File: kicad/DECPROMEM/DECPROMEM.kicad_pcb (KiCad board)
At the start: 2 copper layers, 127 x 132.1 mm, 138 parts, among them J10 BDAL08, J100 A15, J101 A16, J102 A17, J103 A18, J104 A19, J105 A20, J106 A21, J107 +5V, J11 BDAL09, J12 BDAL10, J13 BDAL11, J14 BDAL12, J15 BDAL13, J16 BDAL14, J17 BDAL15, J18 BDAL16, J19 BDAL17, J2 BDAL00, J20 BDAL18, J21 BDAL19, J22 BDAL20, J23 BDAL21, J24 BRPLYL, J25 BMDENL, J26 BWRITEL, J27 BWLBL, J28 BWHBL, J29 BSDENL, J3 BDAL01, J30 SSnL, J31 BDSL, J32 BASL, J33 BIOSELL, J34 BDCOKH, J35 GND, J36 GND, J37 GND, J38 DAH00, J39 DAH01, J4 BDAL02, J40 DAH02, J41 DAH03, J42 DAH04, J43 DAH05, J44 DAH06, J45 DAH07, J46 DAH08, J47 DAH09, J48 DAH10, J49 DAH11, J5 BDAL03, J50 DAH12, J51 DAH13, J52 DAH14, J53 DAH15, J54 DAH16, J55 DAH17, J56 DAH18, J57 DAH19, J58 DAH20, J59 DAH21, J6 BDAL04, J60 JTAG, J61 ASL, J62 MDENL, J63 SDENL, J64 MOEL, J65 MWEL, J66 MCELOWH, J67 MLEL, J68 MCEHIGHL, J69 MHEL, J7 BDAL05, J70 BUSDIR, J71 BUSOE, J72 CLK, J73 MA15, J74 MA16, J75 MA17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

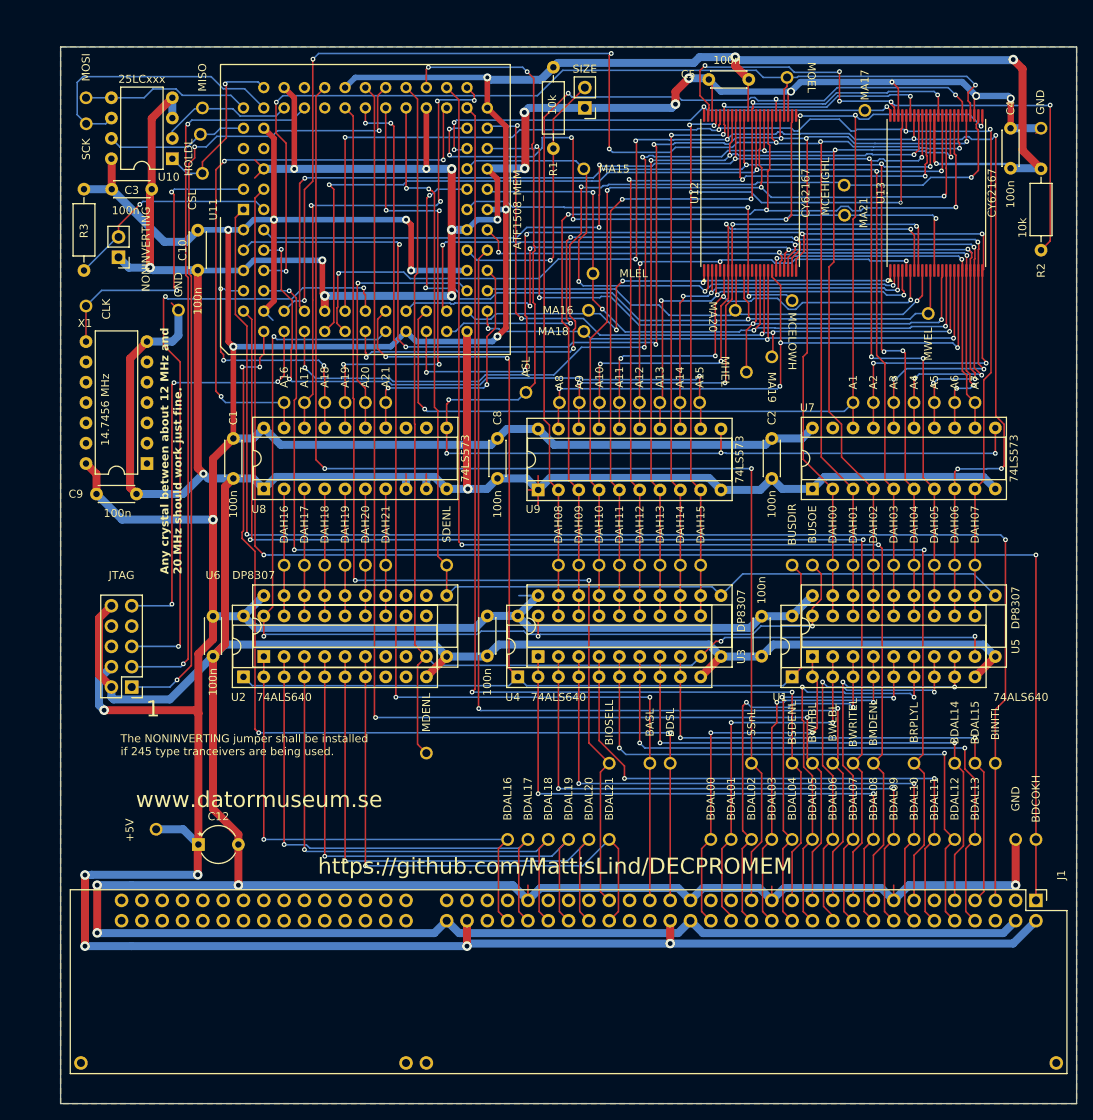
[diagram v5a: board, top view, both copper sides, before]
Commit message: Fixing A - B port mixup on trsnceivers.
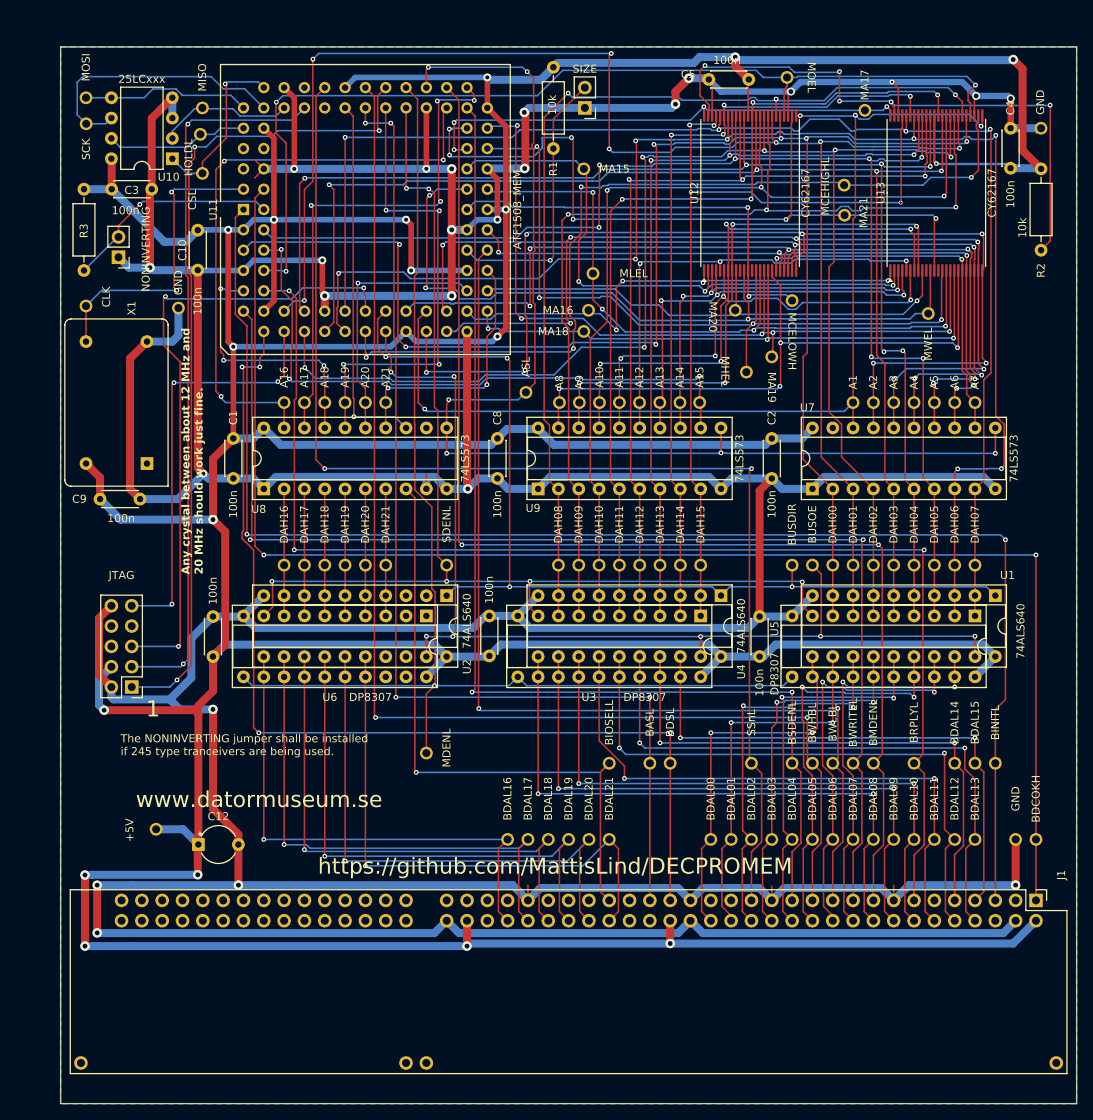
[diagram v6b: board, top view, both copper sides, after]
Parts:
- X1: footprint Package_DIP:DIP-14_W7.62mm -> Oscillator:Oscillator_DIP-14
- moved U4 27.4 mm to (351.8, 182.9), turned to -90 degrees
- moved U1 27.4 mm to (386.1, 182.9), turned to -90 degrees
- moved U2 27.3 mm to (317.5, 182.9), turned to -90 degrees
- moved U3 20.9 mm to (349.2, 185.4), turned to -90 degrees
- moved U5 20.9 mm to (383.5, 185.4), turned to -90 degrees
- moved U6 20.9 mm to (315.0, 185.4), turned to -90 degrees
- moved C6 5.05 mm to (356.6, 190.5), turned to 90 degrees
- moved C7 5.04 mm to (288.3, 190.5), turned to 90 degrees
- moved C11 5.01 mm to (322.8, 190.4), turned to 90 degrees
- moved C9 0.78 mm to (274.2, 170.8)
- moved J36 0.25 mm to (284.0, 146.9)
- moved U9 0.13 mm to (328.9, 169.5)
- turned X1 to 90 degrees
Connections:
- U1 pad 11: /DAH7 -> /BDAL0
- U1 pad 12: /DAH6 -> /BDAL1
- U1 pad 13: /DAH5 -> /BDAL2
- U1 pad 14: /DAH4 -> /BDAL3
- U1 pad 15: /DAH3 -> /BDAL4
- U1 pad 16: /DAH2 -> /BDAL5
- U1 pad 17: /DAH1 -> /BDAL6
- U1 pad 18: /DAH0 -> /BDAL7
- U1 pad 2: /BDAL0 -> /DAH7
- U1 pad 3: /BDAL1 -> /DAH6
- U1 pad 4: /BDAL2 -> /DAH5
- U1 pad 5: /BDAL3 -> /DAH4
- U1 pad 6: /BDAL4 -> /DAH3
- U1 pad 7: /BDAL5 -> /DAH2
- U1 pad 8: /BDAL6 -> /DAH1
- U1 pad 9: /BDAL7 -> /DAH0
- U11 pad 67: /BIOSELL -> Net-(U11-biosel)
- U2 pad 11: unconnected-(U2-B7-Pad11) -> /BDAL16
- U2 pad 12: unconnected-(U2-B6-Pad12) -> /BDAL17
- U2 pad 13: /DAH21 -> /BDAL18
- U2 pad 14: /DAH20 -> /BDAL19
- U2 pad 15: /DAH19 -> /BDAL20
- U2 pad 16: /DAH18 -> /BDAL21
- U2 pad 17: /DAH17 -> unconnected-(U2-B1-Pad17)
- U2 pad 18: /DAH16 -> unconnected-(U2-B0-Pad18)
- U2 pad 2: /BDAL16 -> unconnected-(U2-A0-Pad2)
- U2 pad 3: /BDAL17 -> unconnected-(U2-A1-Pad3)
- U2 pad 4: /BDAL18 -> /DAH21
- U2 pad 5: /BDAL19 -> /DAH20
- U2 pad 6: /BDAL20 -> /DAH19
- U2 pad 7: /BDAL21 -> /DAH18
- U2 pad 8: unconnected-(U2-A6-Pad8) -> /DAH17
- U2 pad 9: unconnected-(U2-A7-Pad9) -> /DAH16
- U3 pad 1: /BDAL8 -> /DAH15
- U3 pad 11: /SDENL -> /MDENL
- U3 pad 12: /DAH15 -> /BDAL8
- U3 pad 13: /DAH14 -> /BDAL9
- U3 pad 14: /DAH13 -> /BDAL10
- U3 pad 15: /DAH12 -> /BDAL11
- U3 pad 16: /DAH11 -> /BDAL12
- U3 pad 17: /DAH10 -> /BDAL13
- U3 pad 18: /DAH9 -> /BDAL14
- U3 pad 19: /DAH8 -> /BDAL15
- U3 pad 2: /BDAL9 -> /DAH14
- U3 pad 3: /BDAL10 -> /DAH13
- U3 pad 4: /BDAL11 -> /DAH12
- U3 pad 5: /BDAL12 -> /DAH11
- U3 pad 6: /BDAL13 -> /DAH10
- U3 pad 7: /BDAL14 -> /DAH9
- U3 pad 8: /BDAL15 -> /DAH8
- U3 pad 9: /MDENL -> /SDENL
- U4 pad 11: /DAH15 -> /BDAL8
- U4 pad 12: /DAH14 -> /BDAL9
- U4 pad 13: /DAH13 -> /BDAL10
- U4 pad 14: /DAH12 -> /BDAL11
- U4 pad 15: /DAH11 -> /BDAL12
- U4 pad 16: /DAH10 -> /BDAL13
- U4 pad 17: /DAH9 -> /BDAL14
- U4 pad 18: /DAH8 -> /BDAL15
- U4 pad 2: /BDAL8 -> /DAH15
- U4 pad 3: /BDAL9 -> /DAH14
- U4 pad 4: /BDAL10 -> /DAH13
- U4 pad 5: /BDAL11 -> /DAH12
- U4 pad 6: /BDAL12 -> /DAH11
- U4 pad 7: /BDAL13 -> /DAH10
- U4 pad 8: /BDAL14 -> /DAH9
- U4 pad 9: /BDAL15 -> /DAH8
- U5 pad 1: /BDAL0 -> /DAH7
- U5 pad 11: /SDENL -> /MDENL
- U5 pad 12: /DAH7 -> /BDAL0
- U5 pad 13: /DAH6 -> /BDAL1
- U5 pad 14: /DAH5 -> /BDAL2
- U5 pad 15: /DAH4 -> /BDAL3
- U5 pad 16: /DAH3 -> /BDAL4
- U5 pad 17: /DAH2 -> /BDAL5
- U5 pad 18: /DAH1 -> /BDAL6
- U5 pad 19: /DAH0 -> /BDAL7
- U5 pad 2: /BDAL1 -> /DAH6
- U5 pad 3: /BDAL2 -> /DAH5
- U5 pad 4: /BDAL3 -> /DAH4
- U5 pad 5: /BDAL4 -> /DAH3
- U5 pad 6: /BDAL5 -> /DAH2
- U5 pad 7: /BDAL6 -> /DAH1
- U5 pad 8: /BDAL7 -> /DAH0
- U5 pad 9: /MDENL -> /SDENL
- U6 pad 1: /BDAL16 -> unconnected-(U6-A0-Pad1)
- U6 pad 11: /SDENL -> /MDENL
- U6 pad 12: unconnected-(U6-B7-Pad12) -> /BDAL16
- U6 pad 13: unconnected-(U6-B6-Pad13) -> /BDAL17
- U6 pad 14: /DAH21 -> /BDAL18
- U6 pad 15: /DAH20 -> /BDAL19
- U6 pad 16: /DAH19 -> /BDAL20
- U6 pad 17: /DAH18 -> /BDAL21
- U6 pad 18: /DAH17 -> unconnected-(U6-B1-Pad18)
- U6 pad 19: /DAH16 -> unconnected-(U6-B0-Pad19)
- U6 pad 2: /BDAL17 -> unconnected-(U6-A1-Pad2)
- U6 pad 3: /BDAL18 -> /DAH21
- U6 pad 4: /BDAL19 -> /DAH20
- U6 pad 5: /BDAL20 -> /DAH19
- U6 pad 6: /BDAL21 -> /DAH18
- U6 pad 7: unconnected-(U6-A6-Pad7) -> /DAH17
- U6 pad 8: unconnected-(U6-A7-Pad8) -> /DAH16
- U6 pad 9: /MDENL -> /SDENL
- U8 pad 13: unconnected-(U8-Q6-Pad13) -> Net-(U11-biosel)
- U8 pad 8: GND -> /BIOSELL
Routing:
- net /BIOSELL: track 130.8 -> 78.6 mm, vias 2 -> 1
- net Net-(U11-biosel): track 0.00 -> 46.2 mm, vias 0 -> 1
- net GND: track 879.4 -> 850.8 mm, vias 23 -> 24
- net +5V: track 723.7 -> 751.3 mm
- net /BUSDIRH: track 147.5 -> 123.6 mm, vias 2 -> 4
- net /SDENL: track 136.5 -> 143.7 mm, vias 2 -> 6
- net /MDENL: track 158.6 -> 155.9 mm, vias 2 -> 1
- net /BUSOEL: track 133.2 -> 131.9 mm, vias 4 -> 7
